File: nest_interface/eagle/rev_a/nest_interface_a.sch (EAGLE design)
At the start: 111 parts, among them J1 MOLEX_MICRO_USB_B_047346, J10 CONN_BLOCK_2, J11 CONN_BLOCK_2, J12 CONN_BLOCK_2, J13 CONN_BLOCK_2, J14 CONN_BLOCK_3, J15 CONN_BLOCK_3, J16 CONN_BLOCK_7, J17 CONN_BLOCK_7, J18 CONN_BLOCK_8, J19 CONN_BLOCK_8, J2 MOLEX_MICRO_USB_B_047346, J20 CONN_BLOCK_8, J21 CONN_BLOCK_8, J5 PJ-036A-SMT, J6 CONN_BLOCK_2, J7 CONN_BLOCK_2, J8 CONN_BLOCK_2, J9 CONN_BLOCK_2, U1 EPIC-CORE_A, U2 MSP430F1611IPM, U3 FT232RL, U4 FT232RL, U5 MPC1825, U6 TC1262, U7 PCA9575, U8 PCA9575, Y1 FC-135_32.768KA-A3

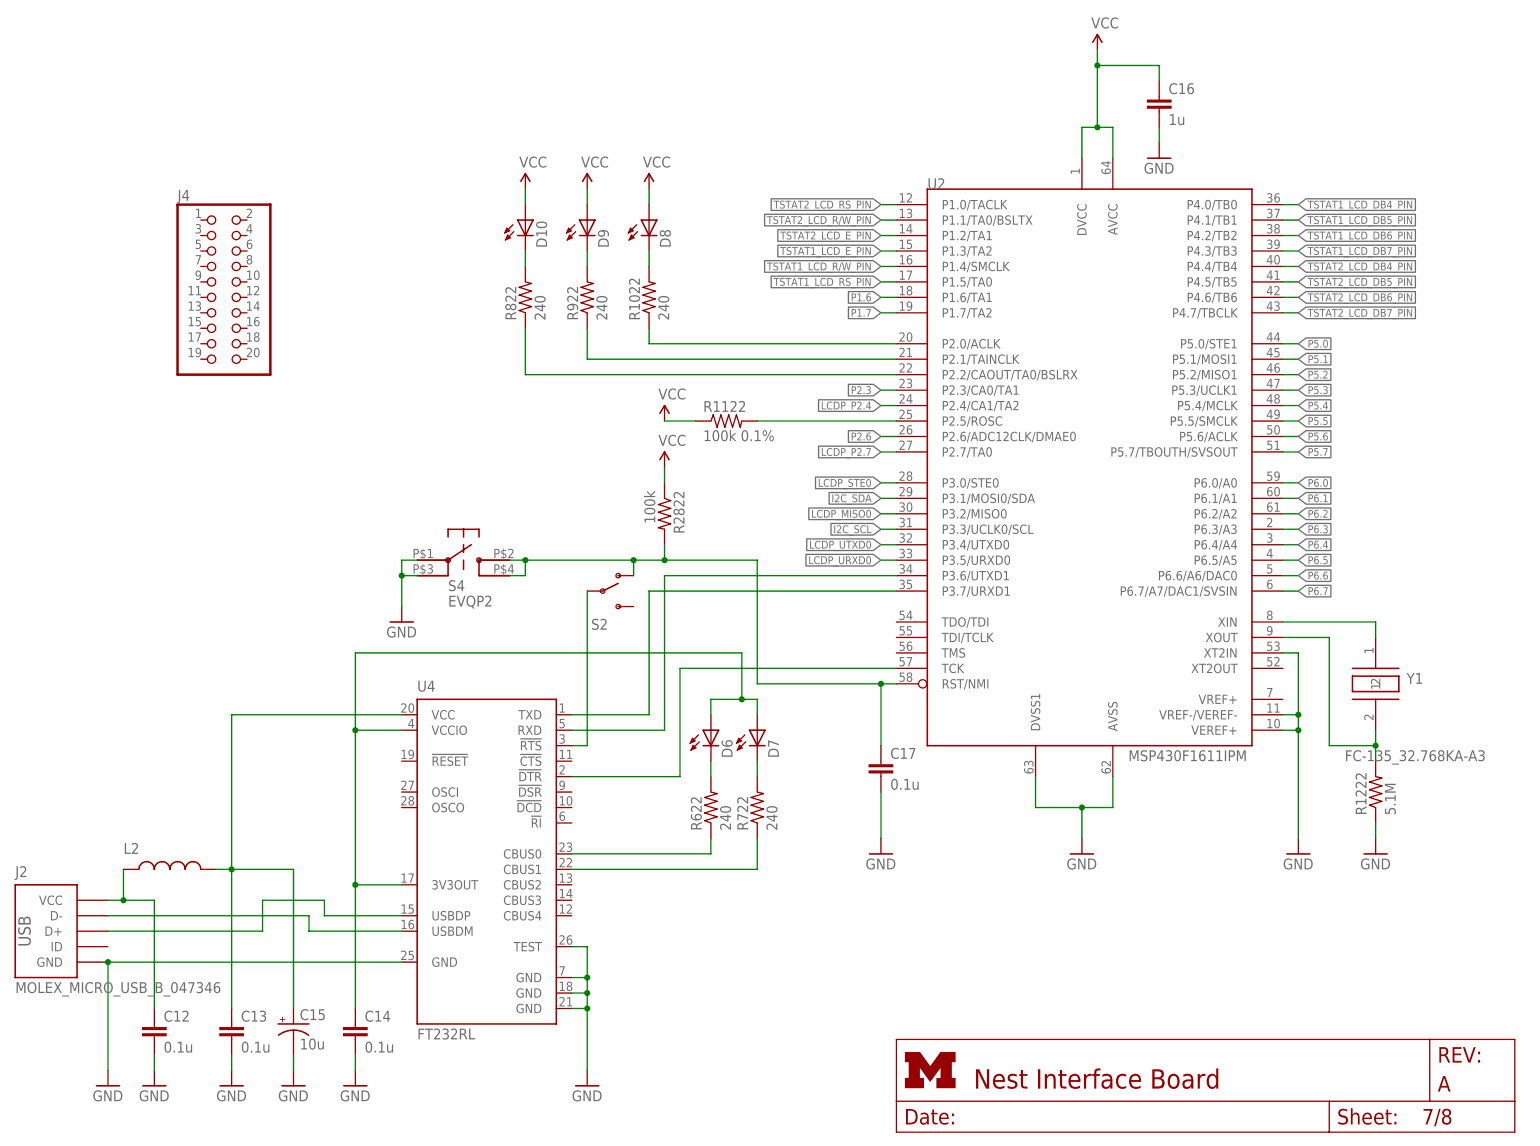
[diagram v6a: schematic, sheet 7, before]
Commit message: labels cleaned up, looks good
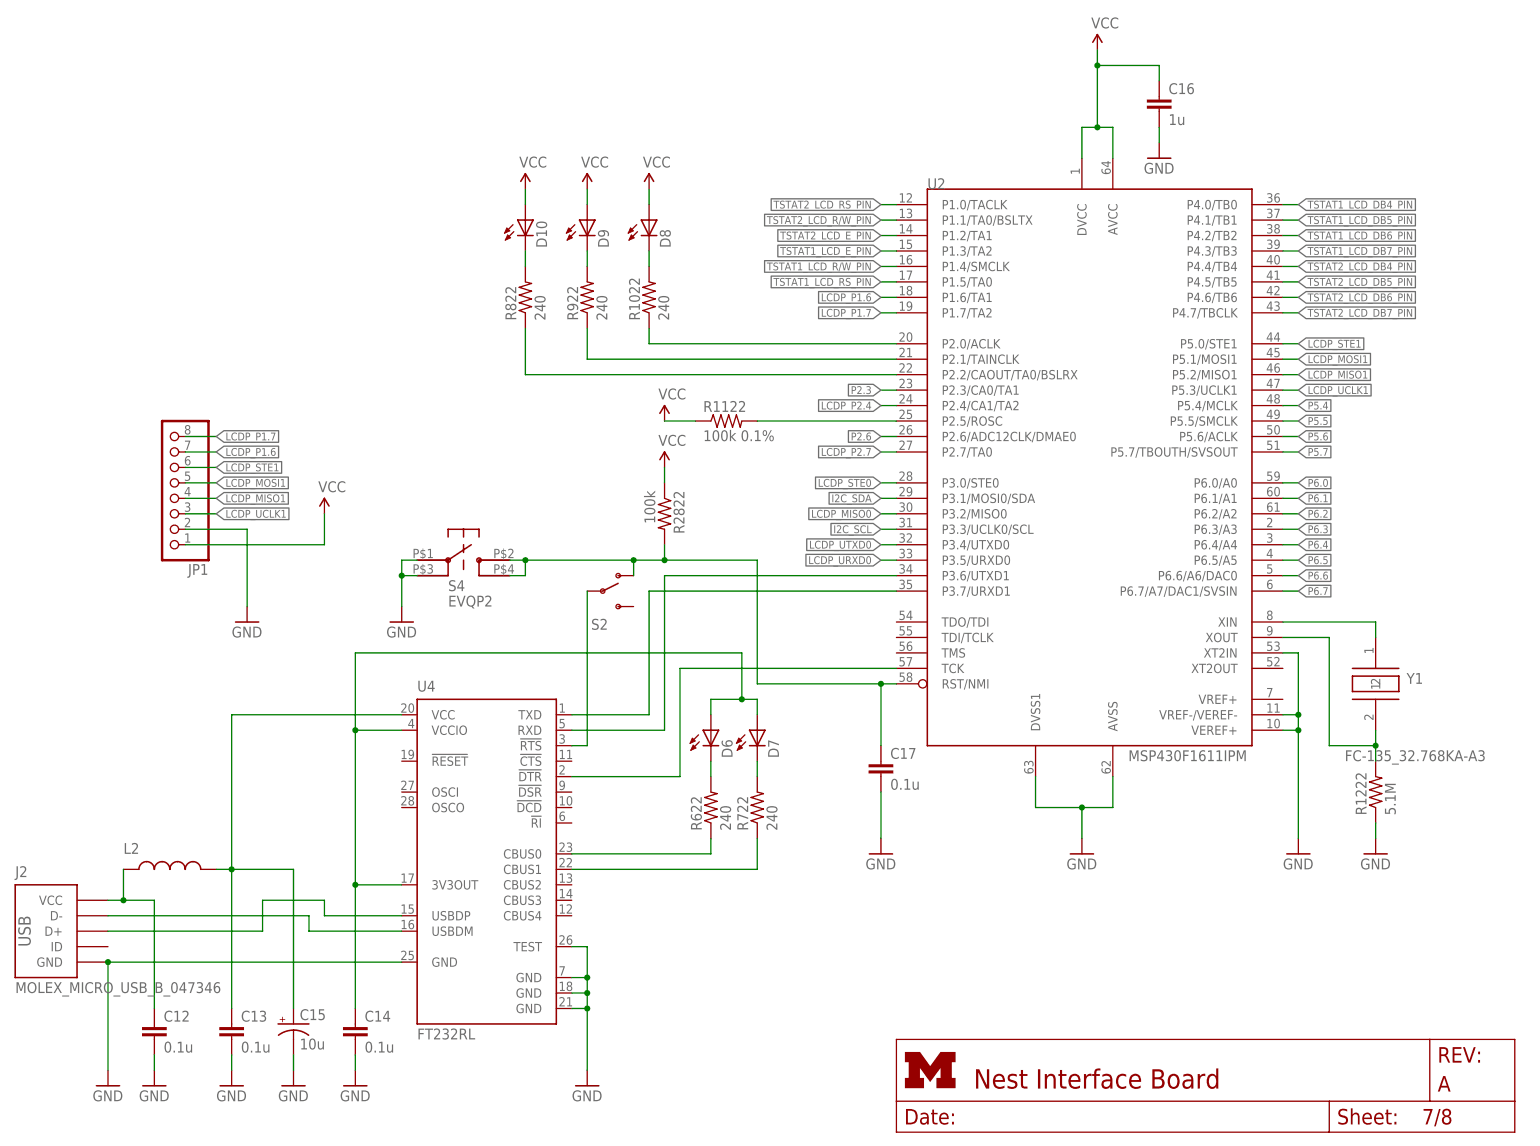
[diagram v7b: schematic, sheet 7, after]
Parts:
- removed J4: (no value), pinhead:PINHD-2X10
- added JP1: (no value), pinhead:PINHD-1X8
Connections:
- removed net P1.6: U2.P1.6/TA1
- removed net P1.7: U2.P1.7/TA2
- removed net P5.0: U2.P5.0/STE1
- removed net P5.1: U2.P5.1/MOSI1
- removed net P5.2: U2.P5.2/MISO1
- removed net P5.3: U2.P5.3/UCLK1
- new net LCDP_MISO1: JP1.4, U2.P5.2/MISO1
- new net LCDP_MOSI1: JP1.5, U2.P5.1/MOSI1
- new net LCDP_P1.6: JP1.7, U2.P1.6/TA1
- new net LCDP_P1.7: JP1.8, U2.P1.7/TA2
- new net LCDP_STE1: JP1.6, U2.P5.0/STE1
- new net LCDP_UCLK1: JP1.3, U2.P5.3/UCLK1
- net GND: now also JP1.2
- net VCC: now also JP1.1
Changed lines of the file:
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@@
 <part name="FRAME7" library="nest_interface" deviceset="LETTER_L" device=""/>
 <part name="FRAME8" library="nest_interface" deviceset="LETTER_L" device=""/>
-<part name="J4" library="pinhead" deviceset="PINHD-2X10" device=""/>
+<part name="JP1" library="pinhead" deviceset="PINHD-1X8" device=""/>
+<part name="GND19" library="supply1" deviceset="GND" device=""/>
+<part name="P+17" library="SparkFun" deviceset="VCC" device=""/>
 </parts>
 <sheets>
@@
 <instance part="FRAME7" gate="G$1" x="0" y="0"/>
 <instance part="FRAME7" gate="G$2" x="147.32" y="0"/>
-<instance part="J4" gate="A" x="35.56" y="139.7"/>
+<instance part="JP1" gate="A" x="27.94" y="106.68" rot="R180"/>
+<instance part="GND19" gate="1" x="40.64" y="83.82"/>
+<instance part="P+17" gate="1" x="53.34" y="101.6"/>
 </instances>
 <busses>
@@
 <wire x1="86.36" y1="154.94" x2="86.36" y2="152.4" width="0.1524" layer="91"/>
 </segment>
+<segment>
+<pinref part="JP1" gate="A" pin="1"/>
+<wire x1="30.48" y1="96.52" x2="53.34" y2="96.52" width="0.1524" layer="91"/>
+<wire x1="53.34" y1="96.52" x2="53.34" y2="101.6" width="0.1524" layer="91"/>
+<pinref part="P+17" gate="1" pin="VCC"/>
+</segment>
 </net>
 <net name="GND" class="0">
@@
 <wire x1="190.5" y1="162.56" x2="190.5" y2="165.1" width="0.1524" layer="91"/>
 </segment>
+<segment>
+<pinref part="JP1" gate="A" pin="2"/>
+<wire x1="30.48" y1="99.06" x2="40.64" y2="99.06" width="0.1524" layer="91"/>
+<wire x1="40.64" y1="99.06" x2="40.64" y2="86.36" width="0.1524" layer="91"/>
+<pinref part="GND19" gate="1" pin="GND"/>
+</segment>
 </net>
 <net name="N$39" class="0">
@@
 </segment>
 </net>
-<net name="P5.0" class="0">
+<net name="LCDP_STE1" class="0">
 <segment>
 <pinref part="U2" gate="G$1" pin="P5.0/STE1"/>
@@
 <label x="213.36" y="129.54" size="1.27" layer="95" xref="yes"/>
 </segment>
+<segment>
+<pinref part="JP1" gate="A" pin="6"/>
+<wire x1="30.48" y1="109.22" x2="35.56" y2="109.22" width="0.1524" layer="91"/>
+<label x="35.56" y="109.22" size="1.27" layer="95" xref="yes"/>
+</segment>
 </net>
-<net name="P5.1" class="0">
+<net name="LCDP_MOSI1" class="0">
 <segment>
 <pinref part="U2" gate="G$1" pin="P5.1/MOSI1"/>
@@
 <label x="213.36" y="127" size="1.27" layer="95" xref="yes"/>
 </segment>
+<segment>
+<pinref part="JP1" gate="A" pin="5"/>
+<wire x1="30.48" y1="106.68" x2="35.56" y2="106.68" width="0.1524" layer="91"/>
+<label x="35.56" y="106.68" size="1.27" layer="95" xref="yes"/>
+</segment>
 </net>
-<net name="P5.2" class="0">
+<net name="LCDP_MISO1" class="0">
 <segment>
 <pinref part="U2" gate="G$1" pin="P5.2/MISO1"/>
@@
 <label x="213.36" y="124.46" size="1.27" layer="95" xref="yes"/>
 </segment>
+<segment>
+<pinref part="JP1" gate="A" pin="4"/>
+<wire x1="30.48" y1="104.14" x2="35.56" y2="104.14" width="0.1524" layer="91"/>
+<label x="35.56" y="104.14" size="1.27" layer="95" xref="yes"/>
+</segment>
 </net>
-<net name="P5.3" class="0">
+<net name="LCDP_UCLK1" class="0">
 <segment>
 <pinref part="U2" gate="G$1" pin="P5.3/UCLK1"/>
@@
 <label x="213.36" y="121.92" size="1.27" layer="95" xref="yes"/>
 </segment>
+<segment>
+<pinref part="JP1" gate="A" pin="3"/>
+<wire x1="30.48" y1="101.6" x2="35.56" y2="101.6" width="0.1524" layer="91"/>
+<label x="35.56" y="101.6" size="1.27" layer="95" xref="yes"/>
+</segment>
 </net>
 <net name="P5.4" class="0">
@@
 </segment>
 </net>
-<net name="P1.6" class="0">
+<net name="LCDP_P1.6" class="0">
 <segment>
 <pinref part="U2" gate="G$1" pin="P1.6/TA1"/>
@@
 <label x="144.78" y="137.16" size="1.27" layer="95" rot="R180" xref="yes"/>
 </segment>
+<segment>
+<pinref part="JP1" gate="A" pin="7"/>
+<wire x1="30.48" y1="111.76" x2="35.56" y2="111.76" width="0.1524" layer="91"/>
+<label x="35.56" y="111.76" size="1.27" layer="95" xref="yes"/>
+</segment>
 </net>
-<net name="P1.7" class="0">
+<net name="LCDP_P1.7" class="0">
 <segment>
 <pinref part="U2" gate="G$1" pin="P1.7/TA2"/>
@@
 <label x="144.78" y="134.62" size="1.27" layer="95" rot="R180" xref="yes"/>
 </segment>
+<segment>
+<pinref part="JP1" gate="A" pin="8"/>
+<wire x1="30.48" y1="114.3" x2="35.56" y2="114.3" width="0.1524" layer="91"/>
+<label x="35.56" y="114.3" size="1.27" layer="95" xref="yes"/>
+</segment>
 </net>

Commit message: added decoupling caps, bom
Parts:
- removed QA8: ALD1107, nest_interface:ALD1107
- added C18, C19: 0.1u, rcl:C-EUC0603
- added QA4: ALD1107, nest_interface:ALD1107
- C10, C11, C6, C7, C8, C9: value .1u -> 0.1u
- C15: value 10u -> 1u; device SparkFun:CAP_POL1206 -> rcl:C-EUC0603
- C16: value 1u -> 10u; device rcl:C-EUC0603 -> SparkFun:CAP_POL1206
- C17: value 0.1u -> 10u; device rcl:C-EUC0603 -> SparkFun:CAP_POL1206
- C4: value 10u -> 0.1u; device SparkFun:CAP_POL1206 -> rcl:C-EUC0603
- renumbered JP1 to J4, R1022 to R10, R1122 to R11, R1222 to R12, R1322 to R13, R1422 to R14, R1522 to R15, R1622 to R16, R1722 to R17, R1822 to R18, R1922 to R19, R2022 to R20, R2122 to R21, R2322 to R22, R2422 to R23, R2522 to R24, R2622 to R25, R2722 to R26, R2822 to R27, R622 to R6, R722 to R7, R822 to R8, R922 to R9, RA7 to RA6
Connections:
- net #KEYPAD_ENABLE: now also QA4.G1, QA4.G2, QA4.G3, QA4.G4; no longer QA8.G1, QA8.G2, QA8.G3, QA8.G4
- net COOLING1_PIN: now also C6.1; no longer C7.1
- net COOLING2_PIN: now also C9.1; no longer C10.1
- net FAN_PIN: now also C7.1; no longer C8.1
- net GND: now also C15.2, C16.-, C17.-, C18.2, C19.2, C5.2, QA4.GND; no longer C15.-, C16.2, C17.2, C4.-, QA8.GND
- net HEATING1_PIN: now also C5.1; no longer C6.1
- net HEATING2_PIN: now also C8.1; no longer C9.1
- net N$18: now also C4.2; no longer C5.2
- net N$39: now also C11.1; no longer C12.1
- net N$43: now also C12.1, C17.+; no longer C13.1, C15.+
- net N$51: now also C13.1; no longer C14.1
- net N$6: now also C16.+; no longer C4.+
- net RST1: now also C14.1; no longer C17.1
- net STAR_PIN: now also C10.1; no longer C11.1
- net TSTAT1_DOWN_IN: now also QA5.S2; no longer QA6.S2
- net TSTAT1_DOWN_OUT: now also QA5.D2; no longer QA6.D2
- net TSTAT1_ENTER_IN: now also QA5.S3; no longer QA6.S3
- net TSTAT1_ENTER_OUT: now also QA5.D3; no longer QA6.D3
- net TSTAT1_ESC_IN: now also QA4.S4; no longer QA5.S4
- net TSTAT1_ESC_OUT: now also QA4.D4; no longer QA5.D4
- net TSTAT1_HELP_IN: now also QA5.S1; no longer QA6.S1
- net TSTAT1_HELP_OUT: now also QA5.D1; no longer QA6.D1
- net TSTAT1_MENU_IN: now also QA4.S2; no longer QA5.S2
- net TSTAT1_MENU_OUT: now also QA4.D2; no longer QA5.D2
- net TSTAT1_ON/OFF_IN: now also QA4.S1; no longer QA5.S1
- net TSTAT1_ON/OFF_OUT: now also QA4.D1; no longer QA5.D1
- net TSTAT1_SPEAKER_IN: now also QA7.S4; no longer QA8.S4
- net TSTAT1_SPEAKER_OUT: now also QA7.D4; no longer QA8.D4
- net TSTAT1_UP_IN: now also QA4.S3; no longer QA5.S3
- net TSTAT1_UP_OUT: now also QA4.D3; no longer QA5.D3
- net TSTAT2_DOWN_IN: now also QA7.S1; no longer QA8.S1
- net TSTAT2_DOWN_OUT: now also QA7.D1; no longer QA8.D1
- net TSTAT2_ENTER_IN: now also QA7.S2; no longer QA8.S2
- net TSTAT2_ENTER_OUT: now also QA7.D2; no longer QA8.D2
- net TSTAT2_ESC_IN: now also QA6.S3; no longer QA7.S3
- net TSTAT2_ESC_OUT: now also QA6.D3; no longer QA7.D3
- net TSTAT2_HELP_IN: now also QA6.S4; no longer QA7.S4
- net TSTAT2_HELP_OUT: now also QA6.D4; no longer QA7.D4
- net TSTAT2_MENU_IN: now also QA6.S1; no longer QA7.S1
- net TSTAT2_MENU_OUT: now also QA6.D1; no longer QA7.D1
- net TSTAT2_ON/OFF_IN: now also QA5.S4; no longer QA6.S4
- net TSTAT2_ON/OFF_OUT: now also QA5.D4; no longer QA6.D4
- net TSTAT2_SPEAKER_IN: now also QA7.S3; no longer QA8.S3
- net TSTAT2_SPEAKER_OUT: now also QA7.D3; no longer QA8.D3
- net TSTAT2_UP_IN: now also QA6.S2; no longer QA7.S2
- net TSTAT2_UP_OUT: now also QA6.D2; no longer QA7.D2
- net VCC: now also C15.1, C18.1, C19.1, C4.1, QA4.VCC; no longer C16.1, C5.1, QA8.VCC
